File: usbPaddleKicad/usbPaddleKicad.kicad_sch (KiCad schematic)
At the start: 3 parts, among them U1 74HC165, U2 RP2040-ZERO, U3 74HC165

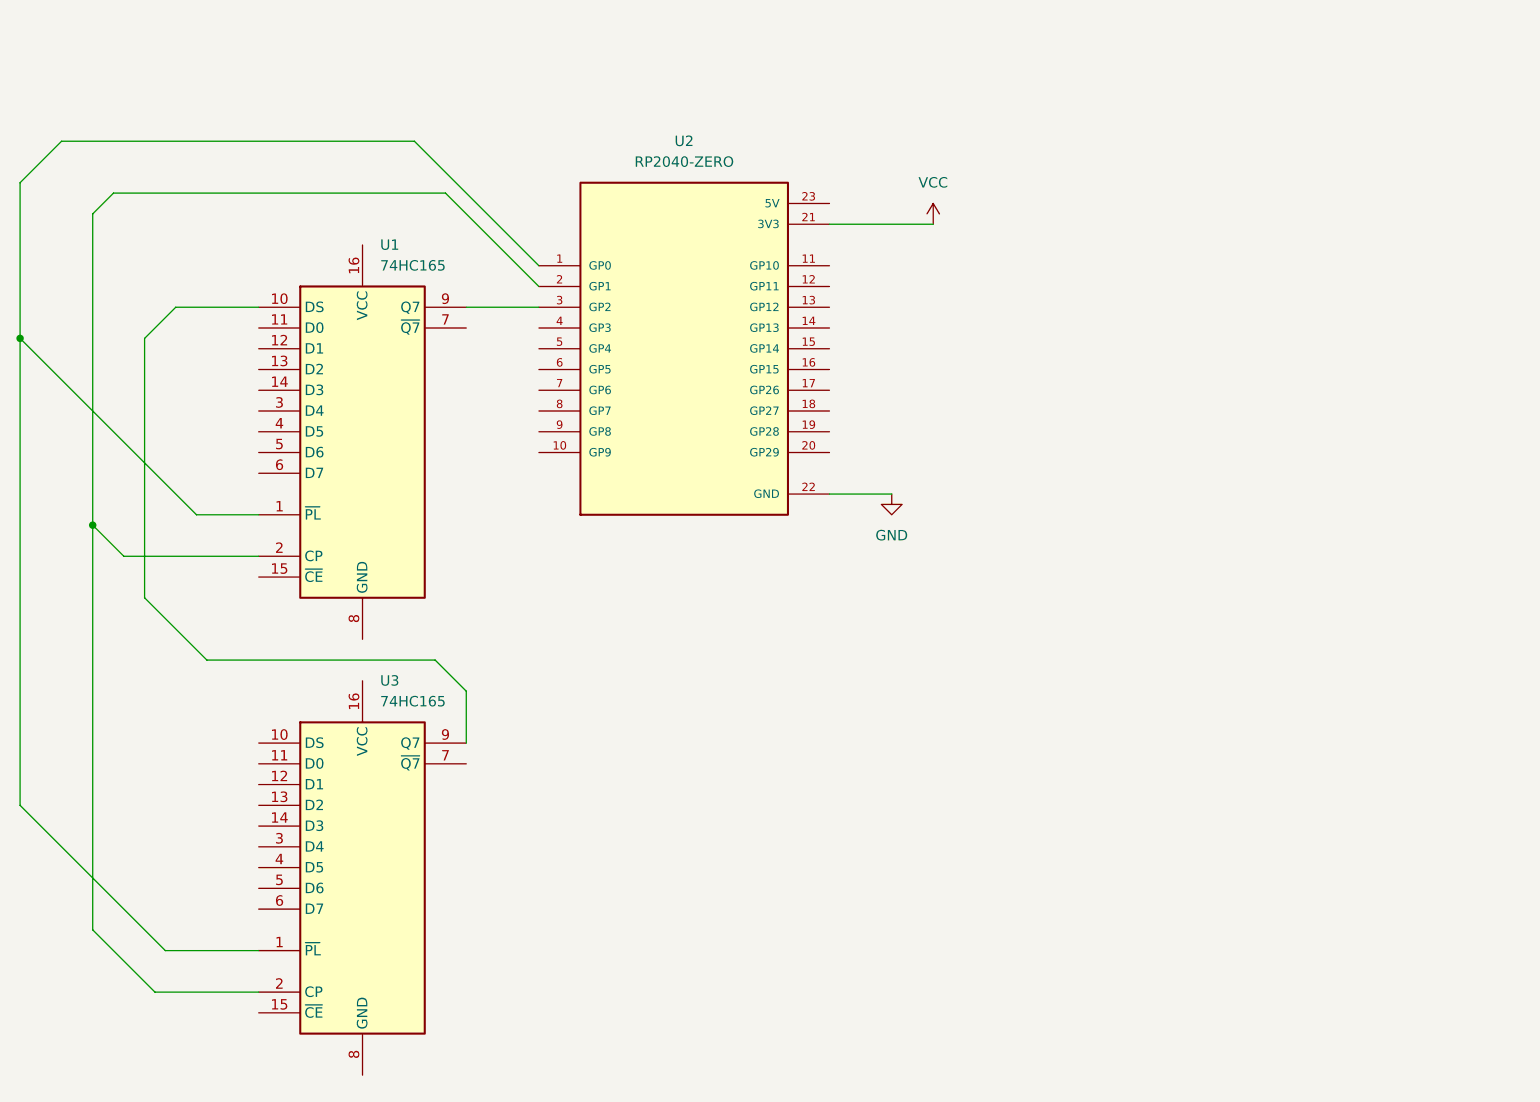
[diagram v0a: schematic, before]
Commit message: wired 4 jacks to rp2040 in schematic
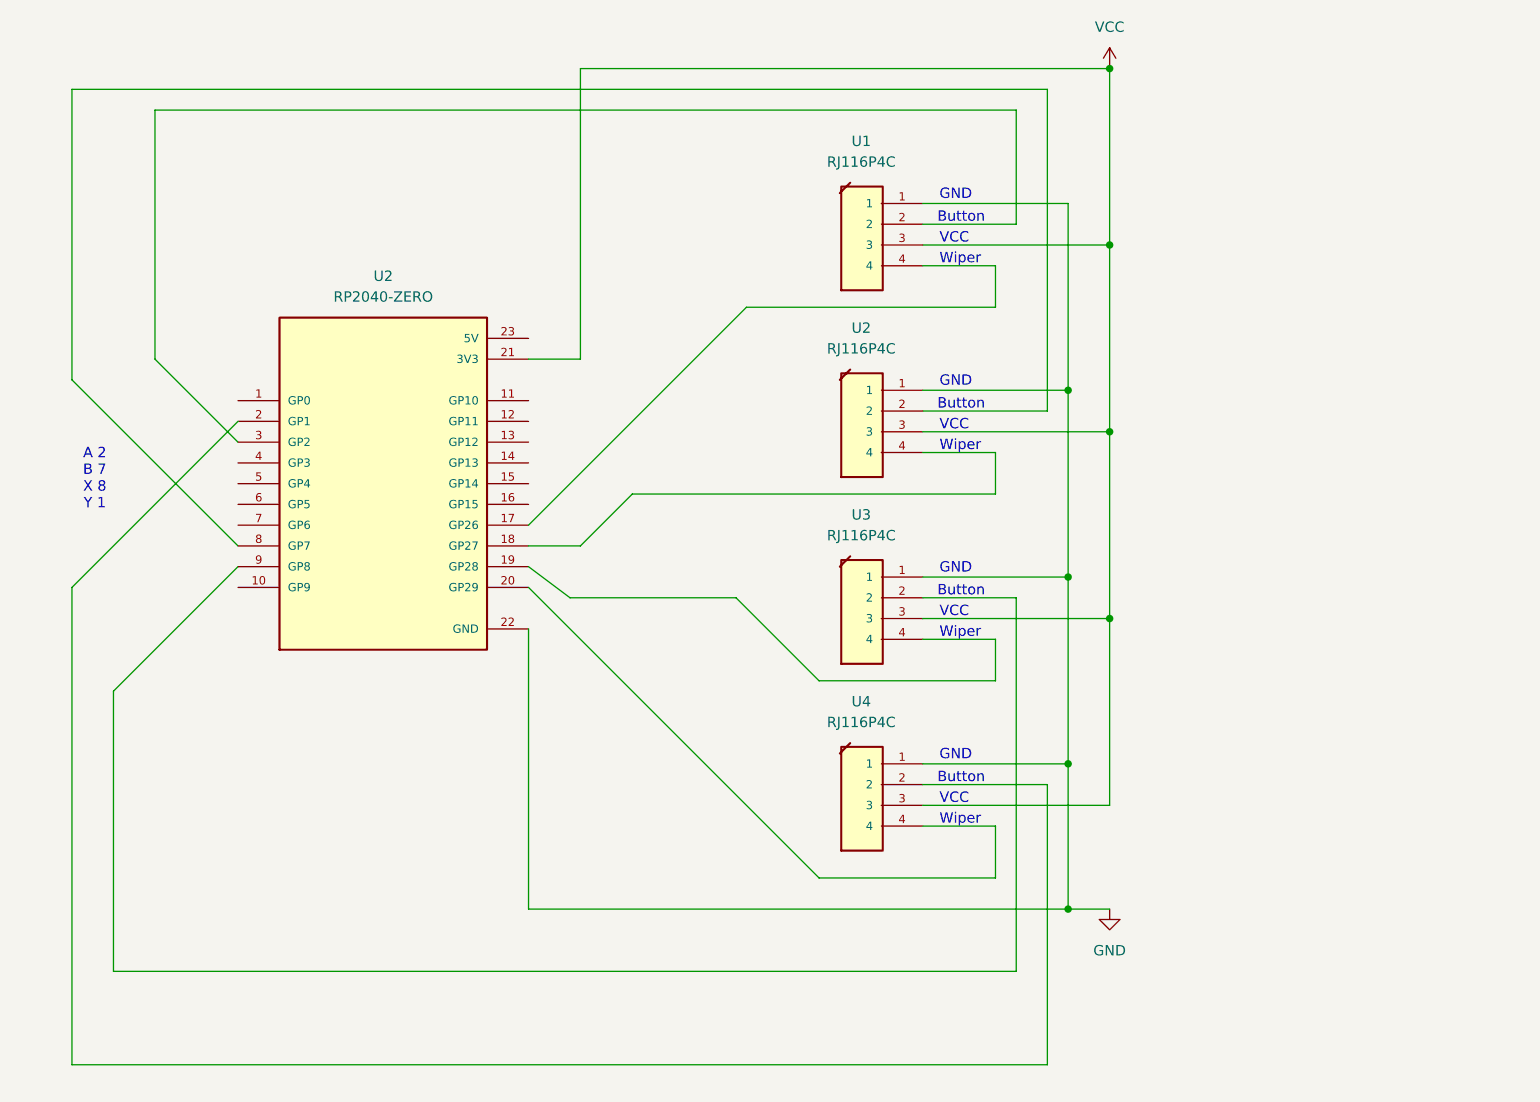
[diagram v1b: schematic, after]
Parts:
- removed U1, U3: 74HC165, symbol 74xx:74HC165
- added U1, U2, U3, U4: RJ116P4C, RJ116P4C:RJ6P4C_GLX-N-64M, symbol RJ116P4C:RJ116P4C
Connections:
- net GND: now also U1.1, U2.1, U3.1, U4.1
- net VCC: now also U1.3, U2.3, U3.3, U4.3
- net at U2.2 (GP1): now also U4.2
- net at U2.3 (GP2): now also U1.2
- net at U2.17 (GP26): now also U1.4
- net at U2.18 (GP27): now also U2.4
- net at U2.19 (GP28): now also U3.4
- net at U2.20 (GP29): now also U4.4
- net at U2.8 (GP7): now also U2.2
- net at U2.9 (GP8): now also U3.2
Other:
- note added: "A 2 B 7 X 8 Y 1"
- note added: "Button"
- note added: "GND"
- note added: "VCC"
- note added: "Wiper"
- moved on the sheet: U2

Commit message: added filter caps and pull-up resistors
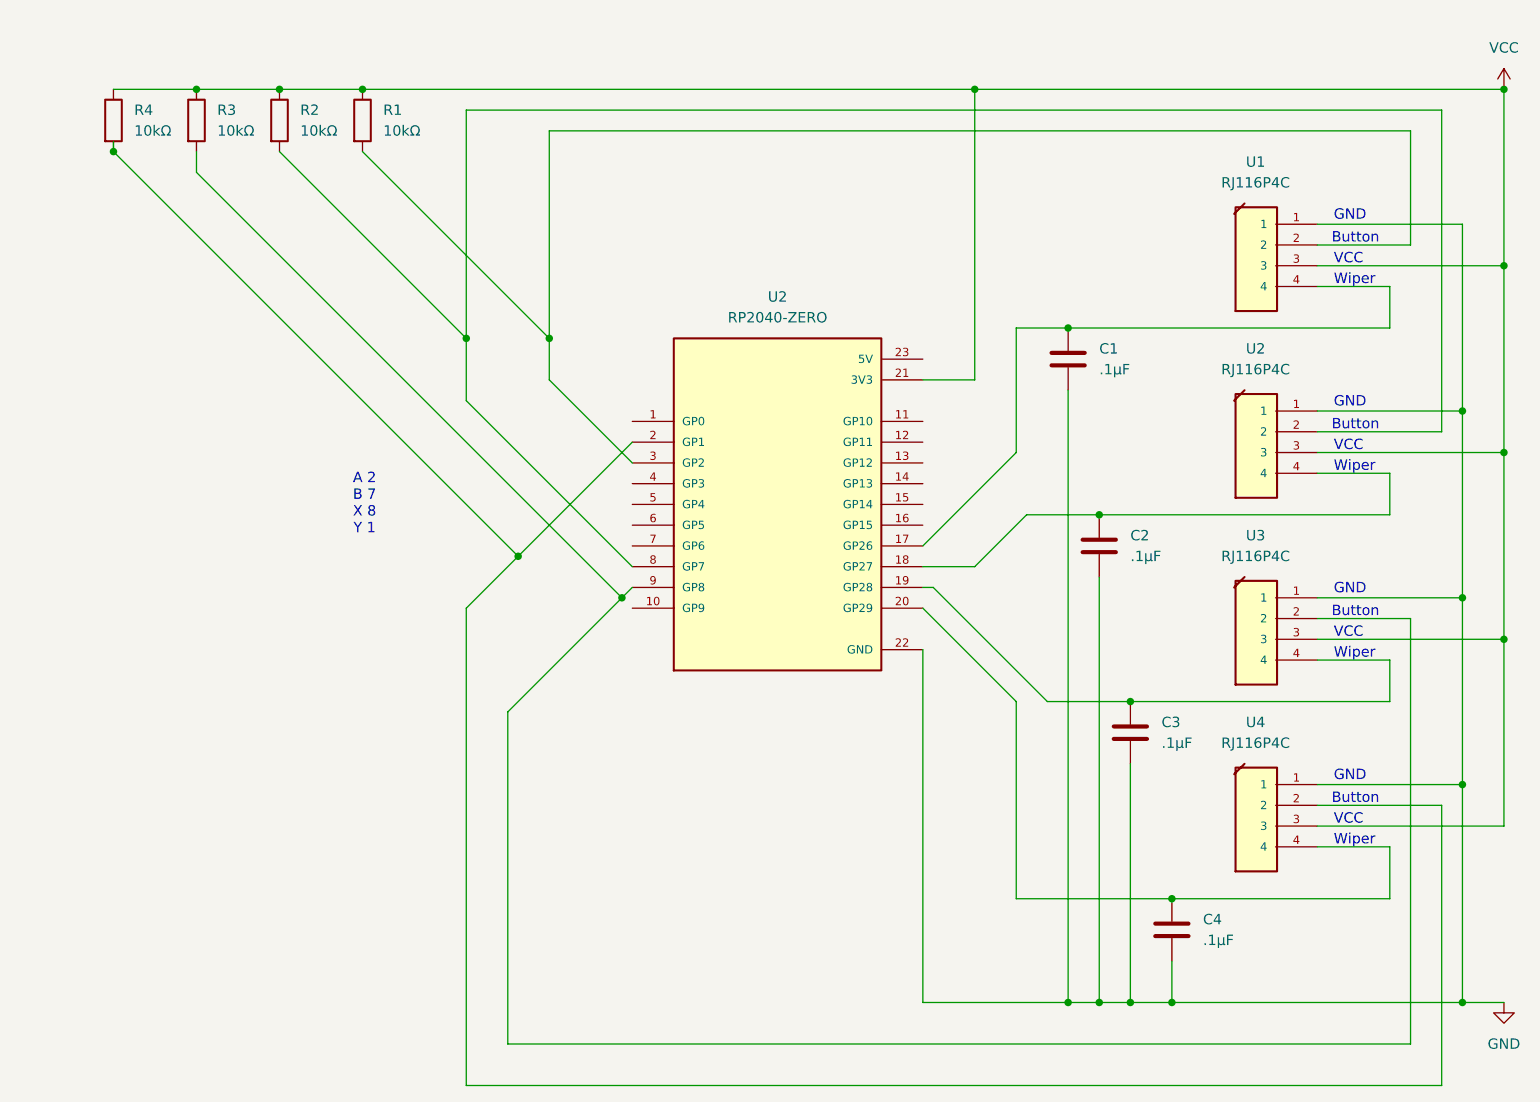
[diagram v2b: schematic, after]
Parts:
- added C1, C2, C3, C4: .1µF, Capacitor_THT:C_Disc_D3.8mm_W2.6mm_P2.50mm, symbol Device:C
- added R1, R2, R3, R4: 10kΩ, Resistor_THT:R_Axial_DIN0309_L9.0mm_D3.2mm_P12.70mm_Horizontal, symbol Device:R
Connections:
- net GND: now also C1.1, C2.1, C3.1, C4.1
- net VCC: now also R1.1, R2.1, R3.1, R4.1
- net at U1.4, U2.17 (GP26): now also C1.2
- net at U2.18 (GP27), U2.4: now also C2.2
- net at U2.19 (GP28), U3.4: now also C3.2
- net at U2.2 (GP1), U4.2: now also R4.2
- net at U2.20 (GP29), U4.4: now also C4.2
- net at U1.2, U2.3 (GP2): now also R1.2
- net at U2.2, U2.8 (GP7): now also R2.2
- net at U2.9 (GP8), U3.2: now also R3.2
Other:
- moved on the sheet: U1, U2, U3, U4

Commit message: pcb layout first pass, not fully routed
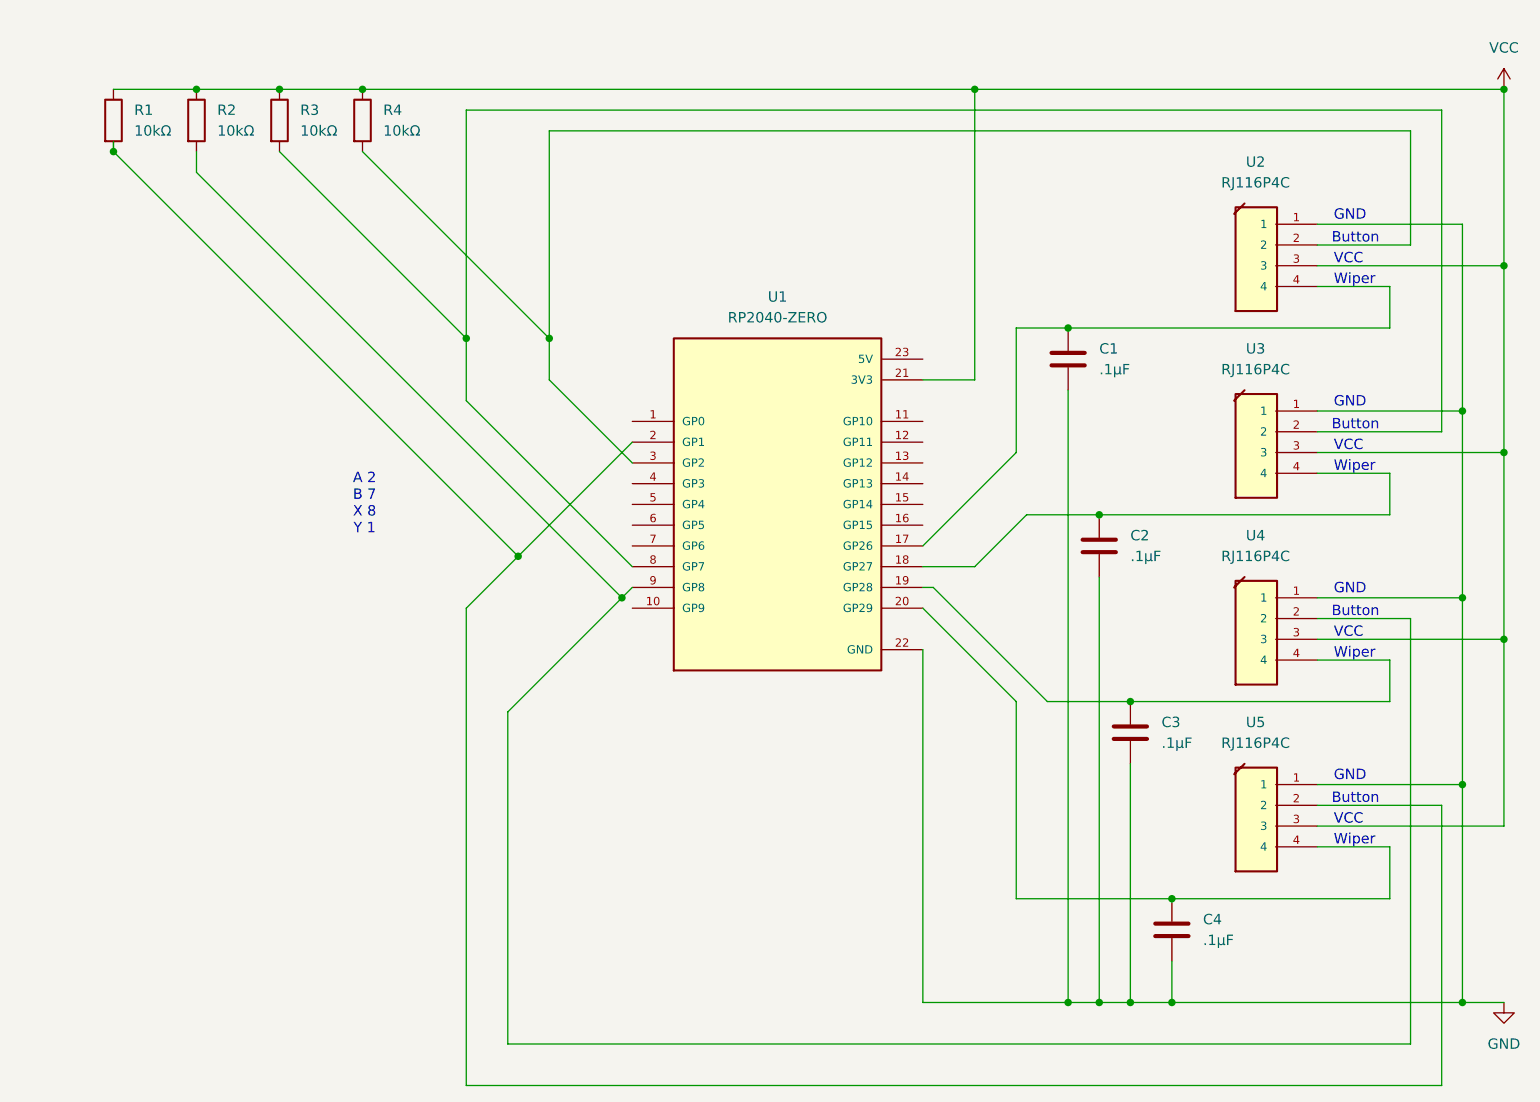
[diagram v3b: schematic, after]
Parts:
- renumbered R4 to R1, R3 to R2, R2 to R3, R1 to R4, U2 to U1, U1 to U2, U2 to U3, U3 to U4, U4 to U5
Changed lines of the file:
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@@
 		(dnp no)
 		(fields_autoplaced yes)
-		(property "Reference" "R3"
+		(property "Reference" "R2"
 			(at 69.85 36.8299 0)
 			(show_name no)
@@
 			(project "usbPaddleKicad"
 				(path "/9df66249-2397-46fa-b5bf-6d1617684761"
-					(reference "R3")
+					(reference "R2")
 					(unit 1)
 				)
@@
 		(dnp no)
 		(fields_autoplaced yes)
-		(property "Reference" "U2"
+		(property "Reference" "U1"
 			(at 138.43 59.69 0)
 			(show_name no)
@@
 			(project "usbPaddleKicad"
 				(path "/9df66249-2397-46fa-b5bf-6d1617684761"
-					(reference "U2")
+					(reference "U1")
 					(unit 1)
 				)
@@
 		(dnp no)
 		(fields_autoplaced yes)
-		(property "Reference" "U1"
+		(property "Reference" "U2"
 			(at 196.9355 43.18 0)
 			(show_name no)
@@
 			(project "usbPaddleKicad"
 				(path "/9df66249-2397-46fa-b5bf-6d1617684761"
-					(reference "U1")
+					(reference "U2")
 					(unit 1)
 				)
@@
 		(dnp no)
 		(fields_autoplaced yes)
-		(property "Reference" "R1"
+		(property "Reference" "R4"
 			(at 90.17 36.8299 0)
 			(show_name no)
@@
 			(project "usbPaddleKicad"
 				(path "/9df66249-2397-46fa-b5bf-6d1617684761"
-					(reference "R1")
+					(reference "R4")
 					(unit 1)
 				)
@@
 		(dnp no)
 		(fields_autoplaced yes)
-		(property "Reference" "R2"
+		(property "Reference" "R3"
 			(at 80.01 36.8299 0)
 			(show_name no)
@@
 			(project "usbPaddleKicad"
 				(path "/9df66249-2397-46fa-b5bf-6d1617684761"
-					(reference "R2")
+					(reference "R3")
 					(unit 1)
 				)
@@
 		(dnp no)
 		(fields_autoplaced yes)
-		(property "Reference" "U3"
+		(property "Reference" "U4"
 			(at 196.9355 88.9 0)
 			(show_name no)
@@
 			(project "usbPaddleKicad"
 				(path "/9df66249-2397-46fa-b5bf-6d1617684761"
-					(reference "U3")
+					(reference "U4")
 					(unit 1)
 				)
@@
 		(dnp no)
 		(fields_autoplaced yes)
-		(property "Reference" "U2"
+		(property "Reference" "U3"
 			(at 196.9355 66.04 0)
 			(show_name no)
@@
 			(project "usbPaddleKicad"
 				(path "/9df66249-2397-46fa-b5bf-6d1617684761"
-					(reference "U2")
+					(reference "U3")
 					(unit 1)
 				)
@@
 		(dnp no)
 		(fields_autoplaced yes)
-		(property "Reference" "U4"
+		(property "Reference" "U5"
 			(at 196.9355 111.76 0)
 			(show_name no)
@@
 			(project "usbPaddleKicad"
 				(path "/9df66249-2397-46fa-b5bf-6d1617684761"
-					(reference "U4")
+					(reference "U5")
 					(unit 1)
 				)
@@
 		(dnp no)
 		(fields_autoplaced yes)
-		(property "Reference" "R4"
+		(property "Reference" "R1"
 			(at 59.69 36.8299 0)
 			(show_name no)
@@
 			(project "usbPaddleKicad"
 				(path "/9df66249-2397-46fa-b5bf-6d1617684761"
-					(reference "R4")
+					(reference "R1")
 					(unit 1)
 				)
